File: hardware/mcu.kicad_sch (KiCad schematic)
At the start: 10 parts, among them J6 PROG, U1 CH32V307WCU6, X1 X50328MSB2GI

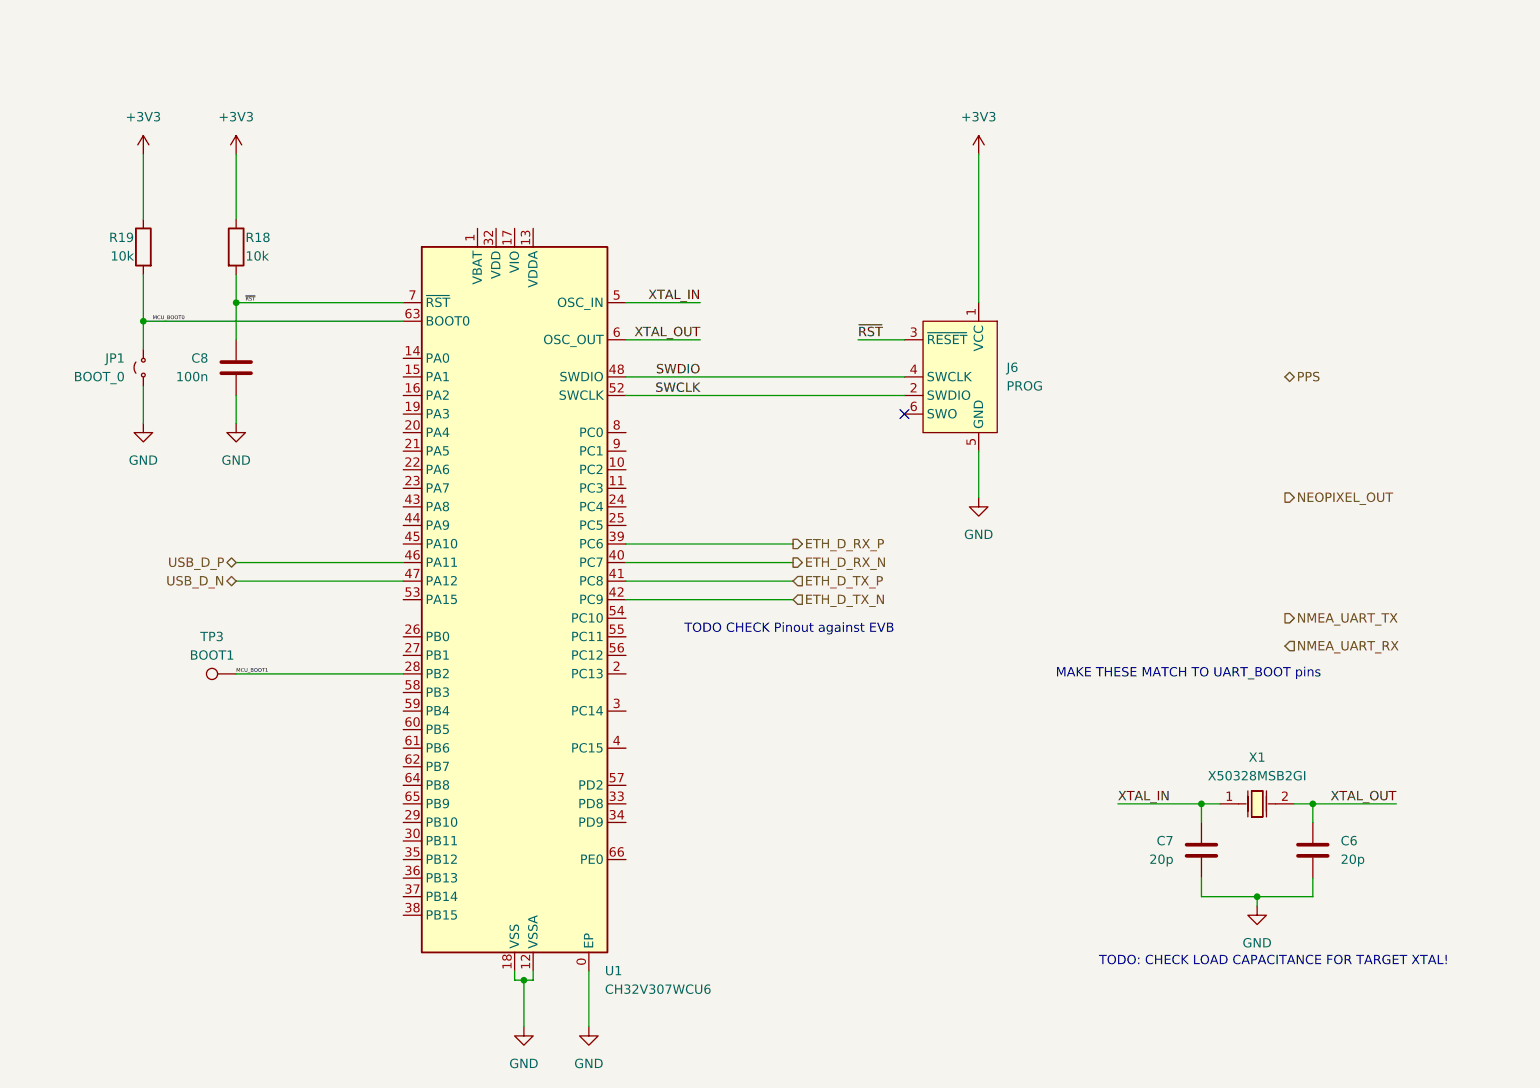
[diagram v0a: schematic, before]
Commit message: Confirm all part footprints, start rought layout
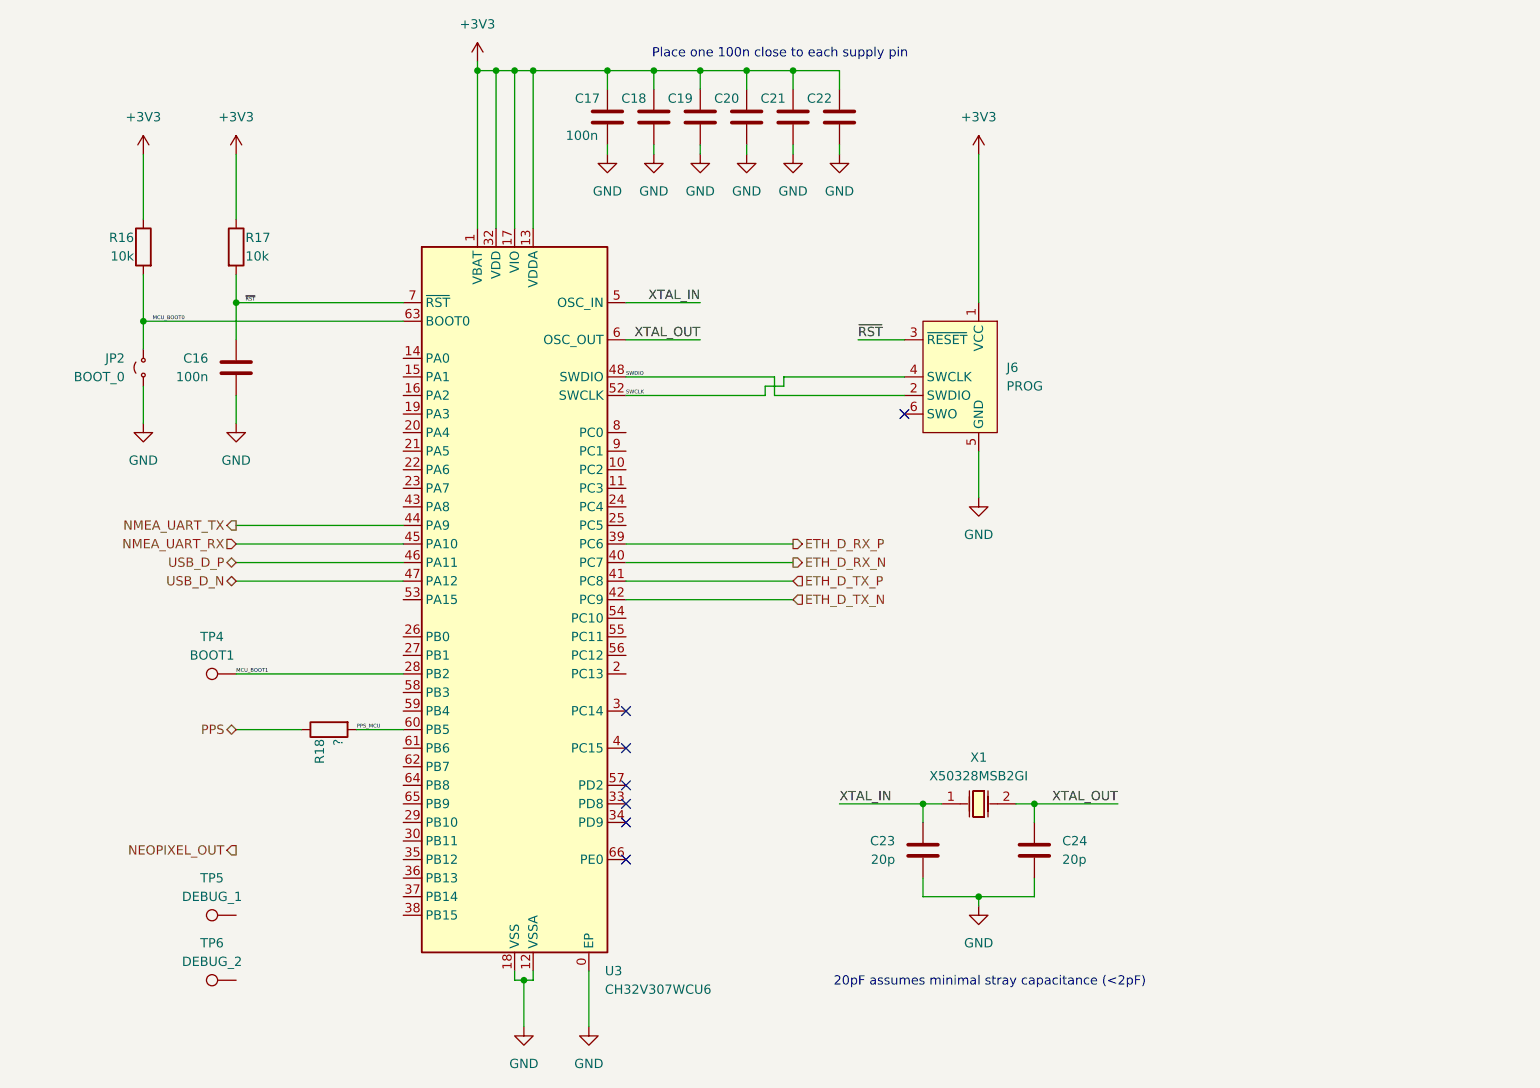
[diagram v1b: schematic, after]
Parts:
- added C17, C18, C19, C20, C21, C22: 100n, Capacitor_SMD:C_0402_1005Metric, symbol Device:C
- added R18: ?, Resistor_SMD:R_0402_1005Metric, symbol Device:R
- added TP5: DEBUG_1, TestPoint:TestPoint_Pad_D1.5mm, symbol Connector:TestPoint
- added TP6: DEBUG_2, TestPoint:TestPoint_Pad_D1.5mm, symbol Connector:TestPoint
- JP2: renamed from JP1; footprint (none) -> Jumper:SolderJumper-2_P1.3mm_Open_RoundedPad1.0x1.5mm
- TP4: renamed from TP3; footprint (none) -> TestPoint:TestPoint_Pad_D1.5mm
- renumbered C8 to C16, C7 to C23, C6 to C24, R19 to R16, R18 to R17, U1 to U3
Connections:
- net +3V3: now also U3.1 (VBAT), U3.13 (VDDA), U3.17 (VIO), U3.31 (VIO), U3.32 (VDD), U3.50 (VDD), U3.51 (VIO), U3.67 (VIO), U3.68 (VDD), C17.1, C18.1, C19.1, C20.1, C21.1, C22.1
- net GND: now also C17.2, C18.2, C19.2, C20.2, C21.2, C22.2
- net NMEA_UART_RX: now also U3.45 (PA10)
- net NMEA_UART_TX: now also U3.44 (PA9)
- net PPS: now also R18.1
- net SWCLK: now also J6.4 (SWCLK); no longer J6.2 (SWDIO)
- net SWDIO: now also J6.2 (SWDIO); no longer J6.4 (SWCLK)
- net PPS_MCU: now reaches U3.60 (PB5)
- net PPS_MCU: now also R18.2
- no-connect marks 1 -> 7
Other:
- note added: "20pF assumes minimal stray capacitance (<2pF)"
- note added: "Place one 100n close to each supply pin"
- note removed: "MAKE THESE MATCH TO UART_BOOT pins"
- note removed: "TODO CHECK Pinout against EVB"
- note removed: "TODO: CHECK LOAD CAPACITANCE FOR TARGET XTAL!"
- moved on the sheet: C23, C24, X1

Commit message: Tidy up layout
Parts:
- renumbered J6 to J7, TP4 to TP2, TP5 to TP3, TP6 to TP4
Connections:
- net NEOPIXEL_OUT: now also U3.36 (PB13)
- net DEBUG_1: now reaches U3.22 (PA6)
- net DEBUG_1: now also TP3.1
- net DEBUG_2: now reaches U3.23 (PA7)
- net DEBUG_2: now also TP4.1
- no-connect marks 7 -> 38
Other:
- moved on the sheet: TP3, TP4

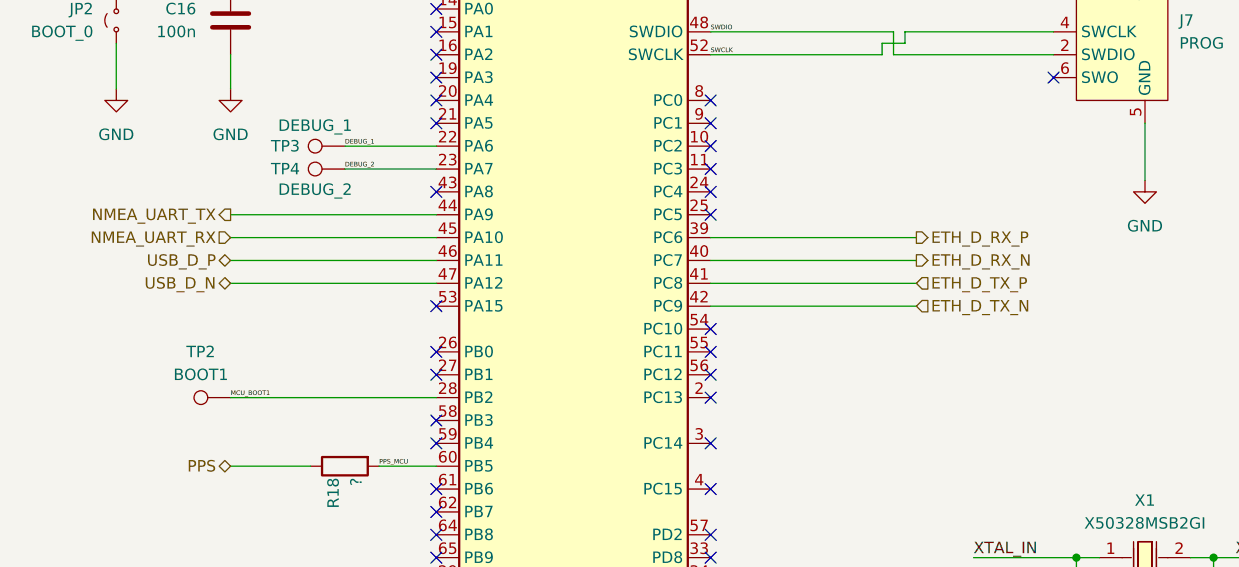
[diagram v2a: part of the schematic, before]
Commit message: All footprints 3D plus some more routing
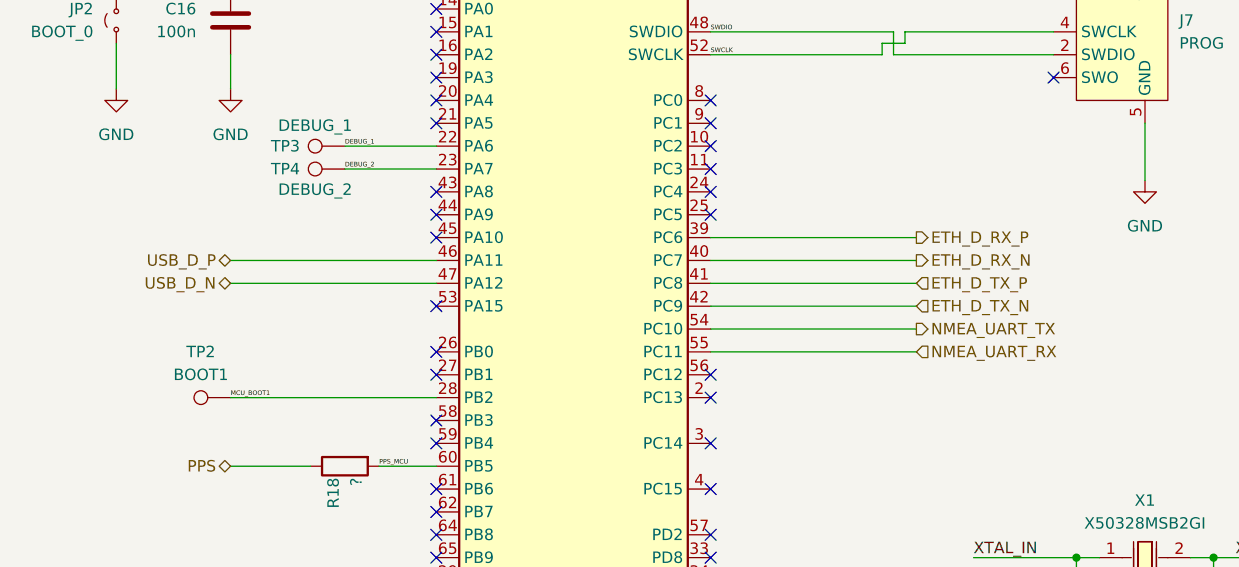
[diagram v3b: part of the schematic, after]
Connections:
- net NMEA_UART_RX: now also U3.55 (PC11); no longer U3.45 (PA10)
- net NMEA_UART_TX: now also U3.54 (PC10); no longer U3.44 (PA9)
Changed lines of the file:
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@@
-	)
-	(no_connect
-		(at 154.94 101.6)
 	)
 	(no_connect
@@
 	)
 	(no_connect
-		(at 154.94 104.14)
-	)
-	(no_connect
 		(at 124.46 111.76)
 	)
@@
 	)
 	(no_connect
+		(at 124.46 88.9)
+	)
+	(no_connect
 		(at 124.46 134.62)
 	)
@@
 	)
 	(no_connect
+		(at 124.46 91.44)
+	)
+	(no_connect
 		(at 154.94 78.74)
 	)
@@
 	(wire
 		(pts
-			(xy 101.6 88.9) (xy 124.46 88.9)
-		)
-		(stroke
-			(width 0)
-			(type default)
-		)
-	)
-	(wire
-		(pts
 			(xy 101.6 137.16) (xy 124.46 137.16)
 		)
@@
 	(wire
 		(pts
+			(xy 154.94 104.14) (xy 177.8 104.14)
+		)
+		(stroke
+			(width 0)
+			(type default)
+		)
+	)
+	(wire
+		(pts
 			(xy 175.26 68.58) (xy 154.94 68.58)
 		)
@@
 	(wire
 		(pts
+			(xy 154.94 101.6) (xy 177.8 101.6)
+		)
+		(stroke
+			(width 0)
+			(type default)
+		)
+	)
+	(wire
+		(pts
 			(xy 186.69 63.5) (xy 193.04 63.5)
 		)
@@
 		(pts
 			(xy 177.8 36.83) (xy 177.8 38.1)
-		)
-		(stroke
-			(width 0)
-			(type default)
-		)
-	)
-	(wire
-		(pts
-			(xy 101.6 91.44) (xy 124.46 91.44)
 		)
 		(stroke
@@
 	(hierarchical_label "NMEA_UART_TX"
 		(shape output)
-		(at 101.6 88.9 180)
+		(at 177.8 101.6 0)
 		(effects
 			(font
 				(size 1.27 1.27)
 			)
-			(justify right)
+			(justify left)
 		)
 	)
@@
 	(hierarchical_label "NMEA_UART_RX"
 		(shape input)
-		(at 101.6 91.44 180)
+		(at 177.8 104.14 0)
 		(effects
 			(font
 				(size 1.27 1.27)
 			)
-			(justify right)
-		)
-	)
+			(justify left)
+		)
+	)

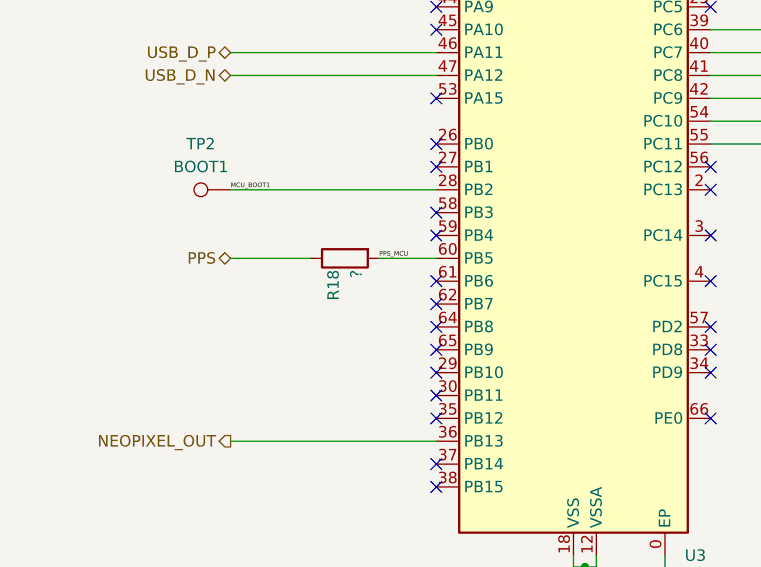
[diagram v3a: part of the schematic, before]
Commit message: Re-link rounded to be default
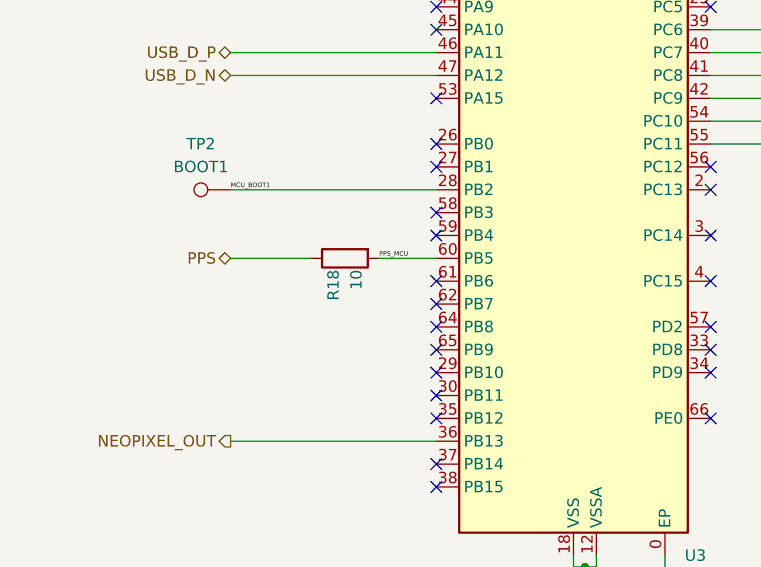
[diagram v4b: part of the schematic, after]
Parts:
- JP2, TP2, TP3, TP4: now left out of the parts list
- R18: value ? -> 10
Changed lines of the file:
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@@
 		(unit 1)
 		(exclude_from_sim no)
-		(in_bom yes)
+		(in_bom no)
 		(on_board yes)
 		(dnp no)
@@
 		(unit 1)
 		(exclude_from_sim no)
-		(in_bom yes)
+		(in_bom no)
 		(on_board yes)
 		(dnp no)
@@
 			)
 		)
-		(property "Value" "?"
+		(property "Value" "10"
 			(at 115.57 118.11 0)
 			(effects
@@
 		(unit 1)
 		(exclude_from_sim no)
-		(in_bom yes)
+		(in_bom no)
 		(on_board yes)
 		(dnp no)
@@
 		(unit 1)
 		(exclude_from_sim no)
-		(in_bom yes)
-		(on_board yes)
-		(dnp no)
+		(in_bom no)
+		(on_board yes)
+		(dnp no)

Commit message: Fix BOM entries, should be good to go
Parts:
- C16, C17, C18, C19, C20, C21, C22: LCSC Part (none) -> C1525
- C23, C24: LCSC Part (none) -> C1554
- R16, R17: LCSC Part (none) -> C25744
- R18: LCSC Part (none) -> C25077
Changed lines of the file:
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@@
+			)
+		)
+		(property "LCSC Part" "C1554"
+			(at 210.82 133.35 0)
+			(effects
+				(font
+					(size 1.27 1.27)
+				)
+				(hide yes)
 			)
 		)
@@
 			)
 		)
+		(property "LCSC Part" "C1525"
+			(at 158.75 33.02 0)
+			(effects
+				(font
+					(size 1.27 1.27)
+				)
+				(hide yes)
+			)
+		)
 		(pin "1"
 		)
@@
 			)
 		)
+		(property "LCSC Part" "C1525"
+			(at 101.6 67.31 0)
+			(effects
+				(font
+					(size 1.27 1.27)
+				)
+				(hide yes)
+			)
+		)
 		(pin "1"
 		)
@@
 			)
 		)
+		(property "LCSC Part" "C1525"
+			(at 177.8 33.02 0)
+			(effects
+				(font
+					(size 1.27 1.27)
+				)
+				(hide yes)
+			)
+		)
 		(pin "1"
 		)
@@
 			)
 		)
+		(property "LCSC Part" "C1525"
+			(at 171.45 33.02 0)
+			(effects
+				(font
+					(size 1.27 1.27)
+				)
+				(hide yes)
+			)
+		)
 		(pin "1"
 		)
@@
 			)
 		)
+		(property "LCSC Part" "C25077"
+			(at 114.3 116.84 0)
+			(effects
+				(font
+					(size 1.27 1.27)
+				)
+				(hide yes)
+			)
+		)
 		(pin "1"
 		)
@@
 			)
 		)
+		(property "LCSC Part" "C1554"
+			(at 195.58 133.35 0)
+			(effects
+				(font
+					(size 1.27 1.27)
+				)
+				(hide yes)
+			)
+		)
 		(pin "1"
 		)
@@
 			)
 		)
+		(property "LCSC Part" "C25744"
+			(at 101.6 50.8 0)
+			(effects
+				(font
+					(size 1.27 1.27)
+				)
+				(hide yes)
+			)
+		)
 		(pin "1"
 		)
@@
 			)
 		)
+		(property "LCSC Part" "C1525"
+			(at 152.4 33.02 0)
+			(effects
+				(font
+					(size 1.27 1.27)
+				)
+				(hide yes)
+			)
+		)
 		(pin "1"
 		)
@@
 			)
 		)
+		(property "LCSC Part" "C1525"
+			(at 165.1 33.02 0)
+			(effects
+				(font
+					(size 1.27 1.27)
+				)
+				(hide yes)
+			)
+		)
 		(pin "1"
 		)
@@
 			)
 		)
+		(property "LCSC Part" "C25744"
+			(at 88.9 50.8 0)
+			(effects
+				(font
+					(size 1.27 1.27)
+				)
+				(hide yes)
+			)
+		)
 		(pin "1"
 		)
@@
 			(at 184.15 33.02 0)
 			(effects
+				(font
+					(size 1.27 1.27)
+				)
+				(hide yes)
+			)
+		)
+		(property "LCSC Part" "C1525"
+			(at 184.15 33.02 0)
+			(effects

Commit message: First of listed hardware changes, need verification
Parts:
- removed JP2: BOOT_0, Jumper:SolderJumper-2_P1.3mm_Open_RoundedPad1.0x1.5mm, symbol Jumper:Jumper_2_Small_Open
- removed TP2: BOOT1, TestPoint:TestPoint_Pad_D1.5mm, symbol Connector:TestPoint
- added Q1: 2N7002, Package_TO_SOT_SMD:SOT-23, symbol Transistor_FET:2N7002
- added R21: 10, Resistor_SMD:R_0402_1005Metric, symbol Device:R
- added R22, R23: 220, Resistor_SMD:R_0603_1608Metric, symbol Device:R
- added R24: 10k, Resistor_SMD:R_0402_1005Metric, symbol Device:R
- added SW1: SW_Push, uPTP:SW-SMD_L3.9-W3.0-P4.45, symbol Switch:SW_Push
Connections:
- net MCU_BOOT1 is gone; now on net GND: U3.28 (PB2)
- net +3V3: now also SW1.2; no longer R16.1
- net GND: now also R16.2, Q1.2 (S)
- net MCU_BOOT0: now also R16.1, SW1.1; no longer R16.2
- net NEOPIXEL_OUT: now also U3.38 (PB15); no longer U3.36 (PB13)
- net PPS: now also R21.1
- net GPS_IN: now reaches U3.58 (PB3)
- net PPS_TIM4_CH1: now reaches U3.61 (PB6)
- net PPS_TIM4_CH1: now also R21.2
- net LOAD_CTRL: now reaches U3.65 (PB9)
- net LOAD_CTRL: now also Q1.1 (G), R24.2
- new net +5V: R22.2, R23.2, R24.1
- new net MPS_LOAD_HS: Q1.3 (D), R22.1, R23.1
- no-connect marks 38 -> 35
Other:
- note added: "POE MPS Load"
- note added: "SPI2_MOSI"
- moved on the sheet: R16, R18

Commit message: Fix pullup
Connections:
- net +3V3: now also R24.1
- net +5V: no longer R24.1
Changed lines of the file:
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@@
 	)
 	(junction
-		(at 251.46 50.8)
-		(diameter 0)
-		(color 0 0 0 0)
-	)
-	(junction
 		(at 210.82 127)
 		(diameter 0)
@@
 	(wire
 		(pts
+			(xy 241.3 38.1) (xy 241.3 53.34)
+		)
+		(stroke
+			(width 0)
+			(type default)
+		)
+	)
+	(wire
+		(pts
 			(xy 134.62 26.67) (xy 137.16 26.67)
 		)
@@
 	(wire
 		(pts
-			(xy 241.3 53.34) (xy 241.3 50.8)
-		)
-		(stroke
-			(width 0)
-			(type default)
-		)
-	)
-	(wire
-		(pts
 			(xy 203.2 38.1) (xy 203.2 58.42)
 		)
@@
 	(wire
 		(pts
-			(xy 241.3 50.8) (xy 251.46 50.8)
-		)
-		(stroke
-			(width 0)
-			(type default)
-		)
-	)
-	(wire
-		(pts
 			(xy 88.9 111.76) (xy 124.46 111.76)
 		)
@@
 					(unit 1)
 				)
+			)
+		)
+	)
+	(symbol
+		(lib_id "power:+3V3")
+		(at 241.3 38.1 0)
+		(unit 1)
+		(exclude_from_sim no)
+		(in_bom yes)
+		(on_board yes)
+		(dnp no)
+		(fields_autoplaced yes)
+		(property "Reference" "#PWR051"
+			(at 241.3 41.91 0)
+			(effects
+				(font
+					(size 1.27 1.27)
+				)
+				(hide yes)
+			)
+		)
+		(property "Value" "+3V3"
+			(at 241.3 33.02 0)
+			(effects
+				(font
+					(size 1.27 1.27)
+				)
+			)
+		)
+		(property "Footprint" ""
+			(at 241.3 38.1 0)
+			(effects
+				(font
+					(size 1.27 1.27)
+				)
+				(hide yes)
+			)
+		)
+		(property "Datasheet" ""
+			(at 241.3 38.1 0)
+			(effects
+				(font
+					(size 1.27 1.27)
+				)
+				(hide yes)
+			)
+		)
+		(property "Description" "Power symbol creates a global label with name \"+3V3\""
+			(at 241.3 38.1 0)
+			(effects
+				(font
+					(size 1.27 1.27)
+				)
+				(hide yes)
+			)
+		)
+		(pin "1"
+		)
+		(instances
+			(project "uPTP"
+				(path "/c29659fd-9e8d-4714-a690-4e74e6e849c2/8b18d07b-35a1-429b-b7b2-9d337819a16d"
+					(reference "#PWR051")
+					(unit 1)
+				)
